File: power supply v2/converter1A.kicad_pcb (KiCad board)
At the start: 2 copper layers, 38.3 x 37.5 mm, 45 parts, among them IC2 LM25145RGYR, IC3 LMR50410YQDBVRQ1, J1 1933189, J3 1933189, J4 Conn_01x04_Pin, Q1 CSD17577Q3A, Q2 CSD17577Q3A

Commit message: last version of pcb and gerber files
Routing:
- net Net-(IC3-EN): track 10.2 -> 11.1 mm
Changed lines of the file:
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@@
 			(plot_on_all_layers_selection 0x00000000_00000000_00000000_00000000)
 			(disableapertmacros no)
-			(usegerberextensions no)
+			(usegerberextensions yes)
 			(usegerberattributes yes)
 			(usegerberadvancedattributes yes)
-			(creategerberjobfile yes)
+			(creategerberjobfile no)
 			(dashed_line_dash_ratio 12.000000)
 			(dashed_line_gap_ratio 3.000000)
@@
 			(sketchdnponfab yes)
 			(crossoutdnponfab yes)
-			(subtractmaskfromsilk no)
+			(subtractmaskfromsilk yes)
 			(outputformat 1)
 			(mirror no)
-			(drillshape 1)
+			(drillshape 0)
 			(scaleselection 1)
-			(outputdirectory "")
+			(outputdirectory "gerber files/")
 		)
 	)
@@
 	)
 	(segment
+		(start 175.75 100.8)
+		(end 175.75 101.75)
+		(width 0.2)
+		(layer "F.Cu")
+		(net 1)
+	)
+	(segment
 		(start 176.875 98.05)
 		(end 177 98.175)
@@
 		(polygon
 			(pts
-				(xy 181.7 84.25) (xy 181.7 84.25) (xy 181.7 91.5) (xy 181.25 91.5) (xy 181.25 93.75) (xy 184.040911 93.75)
-				(xy 187.927275 98.5) (xy 193.2 98.5) (xy 193.2 95) (xy 183.7 86) (xy 183.7 84.25)
+				(xy 181.7 84.25) (xy 181.7 91.5) (xy 181.25 91.5) (xy 181.25 93.75) (xy 184.040911 93.75) (xy 187.927275 98.5)
+				(xy 193.2 98.5) (xy 193.2 95) (xy 183.7 86) (xy 183.7 84.25)
 			)
 		)
@@
 		(polygon
 			(pts
-				(xy 176.25 86.125) (xy 176.5 86.75) (xy 177.75 86.75) (xy 180.5 84) (xy 185 84) (xy 184.959276 81.25)
-				(xy 176.25 81.979072)
+				(xy 176.25 86.125) (xy 176.5 86.75) (xy 177.75 86.75) (xy 180.5 84) (xy 184.5 84) (xy 184.5 81.25)
+				(xy 176.25 81.729072)
 			)
 		)

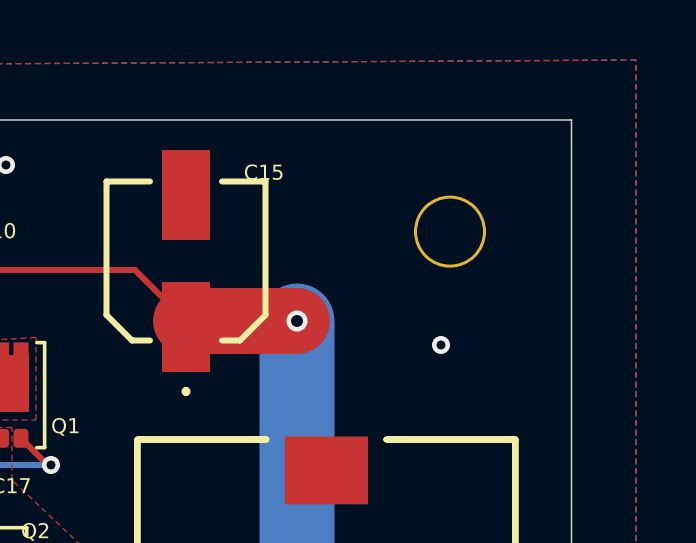
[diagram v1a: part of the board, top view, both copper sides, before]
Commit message: add measurement annotations and move the top right screw up by 0.27mm for standardisation
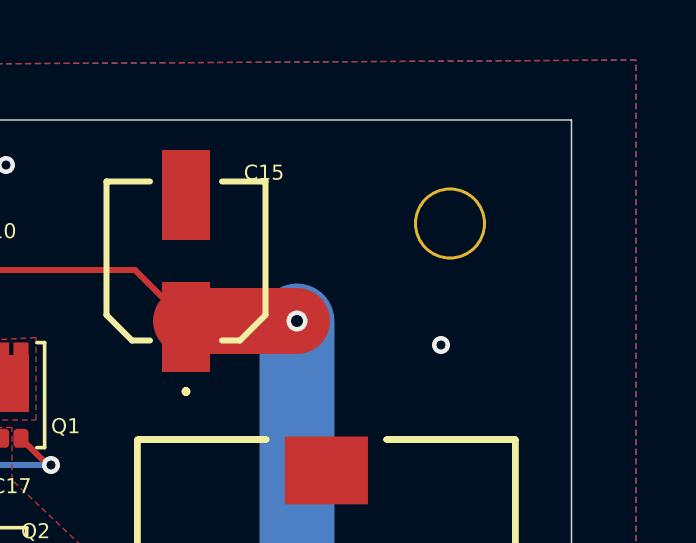
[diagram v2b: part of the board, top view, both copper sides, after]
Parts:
- moved H2 0.27 mm to (198.3, 77.5)
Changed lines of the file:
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@@
 	(footprint "MountingHole:MountingHole_2.2mm_M2"
 		(layer "F.Cu")
-		(at 198.3 77.72)
+		(at 198.3 77.45)
 		(descr "Mounting Hole 2.2mm, no annular, M2")
 		(tags "mounting hole 2.2mm no annular m2")
@@
 		)
 	)
+	(dimension
+		(type orthogonal)
+		(layer "Dwgs.User")
+		(pts
+			(xy 202.35 74) (xy 202.35 111.5)
+		)
+		(height 6.25)
+		(orientation 1)
+		(format
+			(prefix "")
+			(suffix "")
+			(units 3)
+			(units_format 1)
+			(precision 4)
+		)
+		(style
+			(thickness 0.1)
+			(arrow_length 1.27)
+			(text_position_mode 0)
+			(arrow_direction outward)
+			(extension_height 0.58642)
+			(extension_offset 0.5)
+			(keep_text_aligned yes)
+		)
+		(gr_text "37.5000 mm"
+			(at 207.45 92.75 90)
+			(layer "Dwgs.User")
+			(effects
+				(font
+					(size 1 1)
+					(thickness 0.15)
+				)
+			)
+		)
+	)
+	(dimension
+		(type orthogonal)
+		(layer "Dwgs.User")
+		(pts
+			(xy 198.3 77.72) (xy 202.35 77.75)
+		)
+		(height -4.72)
+		(orientation 0)
+		(format
+			(prefix "")
+			(suffix "")
+			(units 3)
+			(units_format 1)
+			(precision 4)
+			(override_value "4.0000")
+		)
+		(style
+			(thickness 0.1)
+			(arrow_length 1.27)
+			(text_position_mode 0)
+			(arrow_direction outward)
+			(extension_height 0.58642)
+			(extension_offset 0.5)
+			(keep_text_aligned yes)
+		)
+		(gr_text "4.0000 mm"
+			(at 200.325 71.85 0)
+			(layer "Dwgs.User")
+			(effects
+				(font
+					(size 1 1)
+					(thickness 0.15)
+				)
+			)
+		)
+	)
+	(dimension
+		(type orthogonal)
+		(layer "Dwgs.User")
+		(pts
+			(xy 168 108) (xy 168.05 111.45)
+		)
+		(height -6.45)
+		(orientation 1)
+		(format
+			(prefix "")
+			(suffix "")
+			(units 3)
+			(units_format 1)
+			(precision 4)
+		)
+		(style
+			(thickness 0.1)
+			(arrow_length 1.27)
+			(text_position_mode 0)
+			(arrow_direction outward)
+			(extension_height 0.58642)
+			(extension_offset 0.5)
+			(keep_text_aligned yes)
+		)
+		(gr_text "3.4500 mm"
+			(at 160.4 109.725 90)
+			(layer "Dwgs.User")
+			(effects
+				(font
+					(size 1 1)
+					(thickness 0.15)
+				)
+			)
+		)
+	)
+	(dimension
+		(type orthogonal)
+		(layer "Dwgs.User")
+		(pts
+			(xy 164 74) (xy 202.35 74)
+		)
+		(height -4.4)
+		(orientation 0)
+		(format
+			(prefix "")
+			(suffix "")
+			(units 3)
+			(units_format 1)
+			(precision 4)
+		)
+		(style
+			(thickness 0.1)
+			(arrow_length 1.27)
+			(text_position_mode 0)
+			(arrow_direction outward)
+			(extension_height 0.58642)
+			(extension_offset 0.5)
+			(keep_text_aligned yes)
+		)
+		(gr_text "38.3500 mm"
+			(at 183.175 68.45 0)
+			(layer "Dwgs.User")
+			(effects
+				(font
+					(size 1 1)
+					(thickness 0.15)
+				)
+			)
+		)
+	)
+	(dimension
+		(type orthogonal)
+		(layer "Dwgs.User")
+		(pts
+			(xy 198.3 77.45) (xy 198.3 74)
+		)
+		(height 7.75)
+		(orientation 1)
+		(format
+			(prefix "")
+			(suffix "")
+			(units 3)
+			(units_format 1)
+			(precision 4)
+		)
+		(style
+			(thickness 0.1)
+			(arrow_length 1.27)
+			(text_position_mode 0)
+			(arrow_direction outward)
+			(extension_height 0.58642)
+			(extension_offset 0.5)
+			(keep_text_aligned yes)
+		)
+		(gr_text "3.4500 mm"
+			(at 204.9 75.725 90)
+			(layer "Dwgs.User")
+			(effects
+				(font
+					(size 1 1)
+					(thickness 0.15)
+				)
+			)
+		)
+	)
+	(dimension
+		(type orthogonal)
+		(layer "Dwgs.User")
+		(pts
+			(xy 168 108) (xy 164 108)
+		)
+		(height 6.7)
+		(orientation 0)
+		(format
+			(prefix "")
+			(suffix "")
+			(units 3)
+			(units_format 1)
+			(precision 4)
+		)
+		(style
+			(thickness 0.1)
+			(arrow_length 1.27)
+			(text_position_mode 0)
+			(arrow_direction outward)
+			(extension_height 0.58642)
+			(extension_offset 0.5)
+			(keep_text_aligned yes)
+		)
+		(gr_text "4.0000 mm"
+			(at 166 113.55 0)
+			(layer "Dwgs.User")
+			(effects
+				(font
+					(size 1 1)
+					(thickness 0.15)
+				)
+			)
+		)
+	)

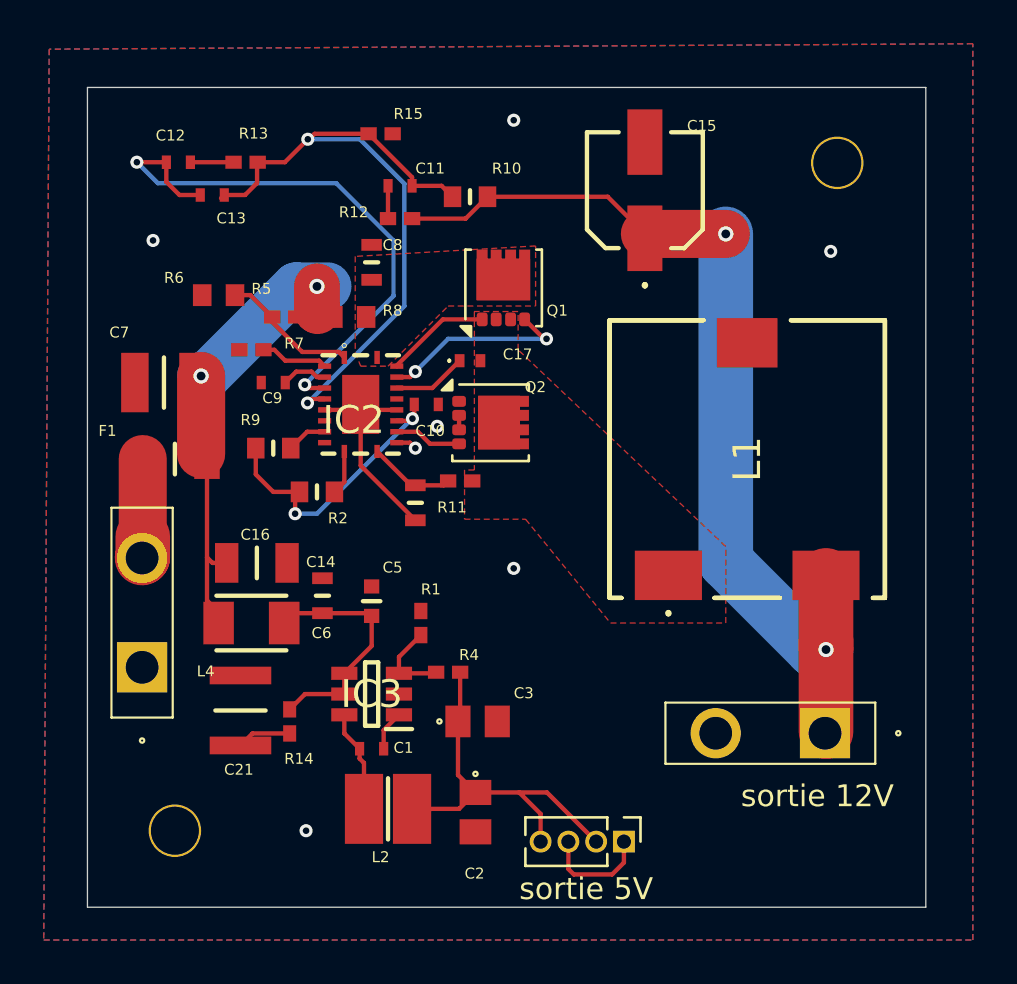
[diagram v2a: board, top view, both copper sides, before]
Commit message: add 2 2.4mm screw holes and regenerate gerber files
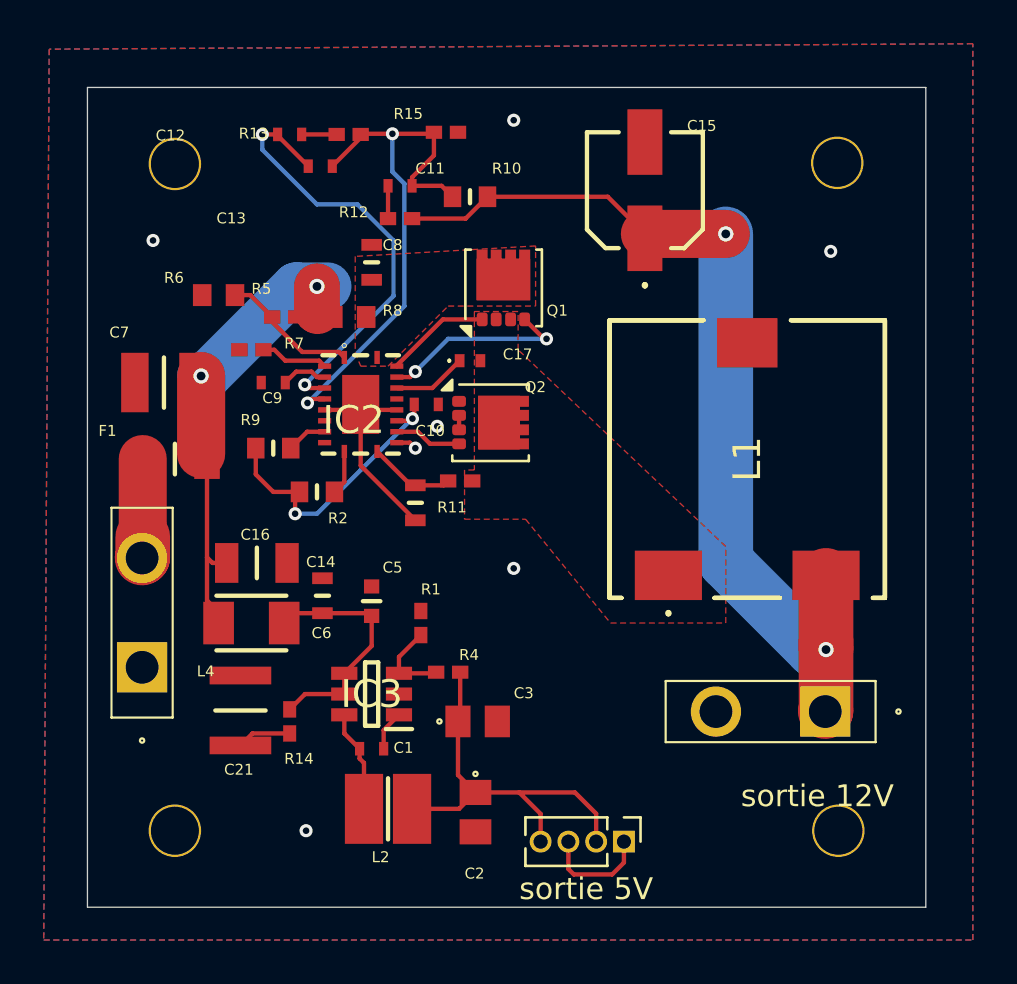
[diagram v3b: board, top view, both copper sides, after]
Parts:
- added H2: MountingHole, MountingHole:MountingHole_2.2mm_M2, F.Cu at (168.0, 77.5)
- added H3: MountingHole, MountingHole:MountingHole_2.2mm_M2, F.Cu at (198.3, 108.0)
- moved C12 5.25 mm to (173.2, 76.2)
- moved C13 5.11 mm to (174.7, 77.6)
- moved R13 4.88 mm to (175.9, 76.2)
- moved R15 2.99 mm to (180.4, 76.0)
- moved J1 0.99 mm to (197.8, 102.5)
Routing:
- net Net-(IC2-FB): track 31.4 -> 25.1 mm
- net Net-(IC2-COMP): track 26.5 -> 20.4 mm
- net Net-(C15-+): track 44.3 -> 43.4 mm
- net Net-(J4-Pin_2): track 18.2 -> 18.9 mm
